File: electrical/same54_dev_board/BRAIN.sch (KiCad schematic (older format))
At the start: 8 parts, among them J2 Conn_ARM_JTAG_SWD_10, U1 p_ATSAME54P20A-AU, Y1 XOSC32

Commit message: Trying to figure out how I want to do power...
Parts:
- J2: footprint Connector_PinSocket_1.27mm:PinSocket_2x04_P1.27mm_Vertical -> Connector_PinHeader_1.27mm:PinHeader_2x05_P1.27mm_Vertical
- gave numbers to parts that had none: 5
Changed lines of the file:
@@
 F 0 "J2" H 5757 5196 50  0000 R CNN
 F 1 "Conn_ARM_JTAG_SWD_10" H 5757 5105 50  0000 R CNN
-F 2 "Connector_PinSocket_1.27mm:PinSocket_2x04_P1.27mm_Vertical" H 6200 5150 50  0001 C CNN
+F 2 "Connector_PinHeader_1.27mm:PinHeader_2x05_P1.27mm_Vertical" H 6200 5150 50  0001 C CNN
 F 3 "http://infocenter.arm.com/help/topic/com.arm.doc.ddi0314h/DDI0314H_coresight_components_trm.pdf" V 5850 3900 50  0001 C CNN
 	1    6200 5150
@@
 $EndComp
 $Comp
-L Device:C_Small C?
+L Device:C_Small C1
 U 1 1 5E7E5146
 P 5100 1050
-F 0 "C?" V 4871 1050 50  0000 C CNN
+F 0 "C1" V 4871 1050 50  0000 C CNN
 F 1 "6.8pF" V 4962 1050 50  0000 C CNN
 F 2 "" H 5100 1050 50  0001 C CNN
@@
 $EndComp
 $Comp
-L Device:C_Small C?
+L Device:C_Small C2
 U 1 1 5E7E6123
 P 5100 1550
-F 0 "C?" V 4871 1550 50  0000 C CNN
+F 0 "C2" V 4871 1550 50  0000 C CNN
 F 1 "6.8pF" V 4950 1500 50  0000 C CNN
 F 2 "" H 5100 1550 50  0001 C CNN
@@
 	5450 1300 5450 1550
 $Comp
-L power:GND #PWR?
+L power:GND #PWR0104
 U 1 1 5E825E8D
 P 5550 1300
-F 0 "#PWR?" H 5550 1050 50  0001 C CNN
+F 0 "#PWR0104" H 5550 1050 50  0001 C CNN
 F 1 "GND" H 5555 1127 50  0000 C CNN
 F 2 "" H 5550 1300 50  0001 C CNN
@@
 Connection ~ 5350 2700
 $Comp
-L power:GND #PWR?
+L power:GND #PWR0108
 U 1 1 5E880A2C
 P 5900 2850
-F 0 "#PWR?" H 5900 2600 50  0001 C CNN
+F 0 "#PWR0108" H 5900 2600 50  0001 C CNN
 F 1 "GND" H 5905 2677 50  0000 C CNN
 F 2 "" H 5900 2850 50  0001 C CNN
@@
 	4900 2750 4250 2750
 $Comp
-L Device:C_Small C?
+L Device:C_Small C5
 U 1 1 5E8AA0A3
 P 5250 3050
-F 0 "C?" V 5450 3050 50  0000 C CNN
+F 0 "C5" V 5450 3050 50  0000 C CNN
 F 1 "5pF" V 5350 3050 50  0000 C CNN
 F 2 "" H 5250 3050 50  0001 C CNN
@@
 	5350 2700 4950 2700
 $Comp
-L Device:Crystal_GND24 Y?
+L Device:Crystal_GND24 Y2
 U 1 1 5E843969
 P 5150 2700
-F 0 "Y?" V 5100 3050 50  0000 R CNN
+F 0 "Y2" V 5100 3050 50  0000 R CNN
 F 1 "XOSC0" V 5000 3200 50  0000 R CNN
 F 2 "" H 5150 2700 50  0001 C CNN
@@
 Connection ~ 5150 2900
 $Comp
-L Device:C_Small C?
+L Device:C_Small C4
 U 1 1 5E8C2D5D
 P 5250 2350
-F 0 "C?" V 5021 2350 50  0000 C CNN
+F 0 "C4" V 5021 2350 50  0000 C CNN
 F 1 "5pF" V 5112 2350 50  0000 C CNN
 F 2 "" H 5250 2350 50  0001 C CNN

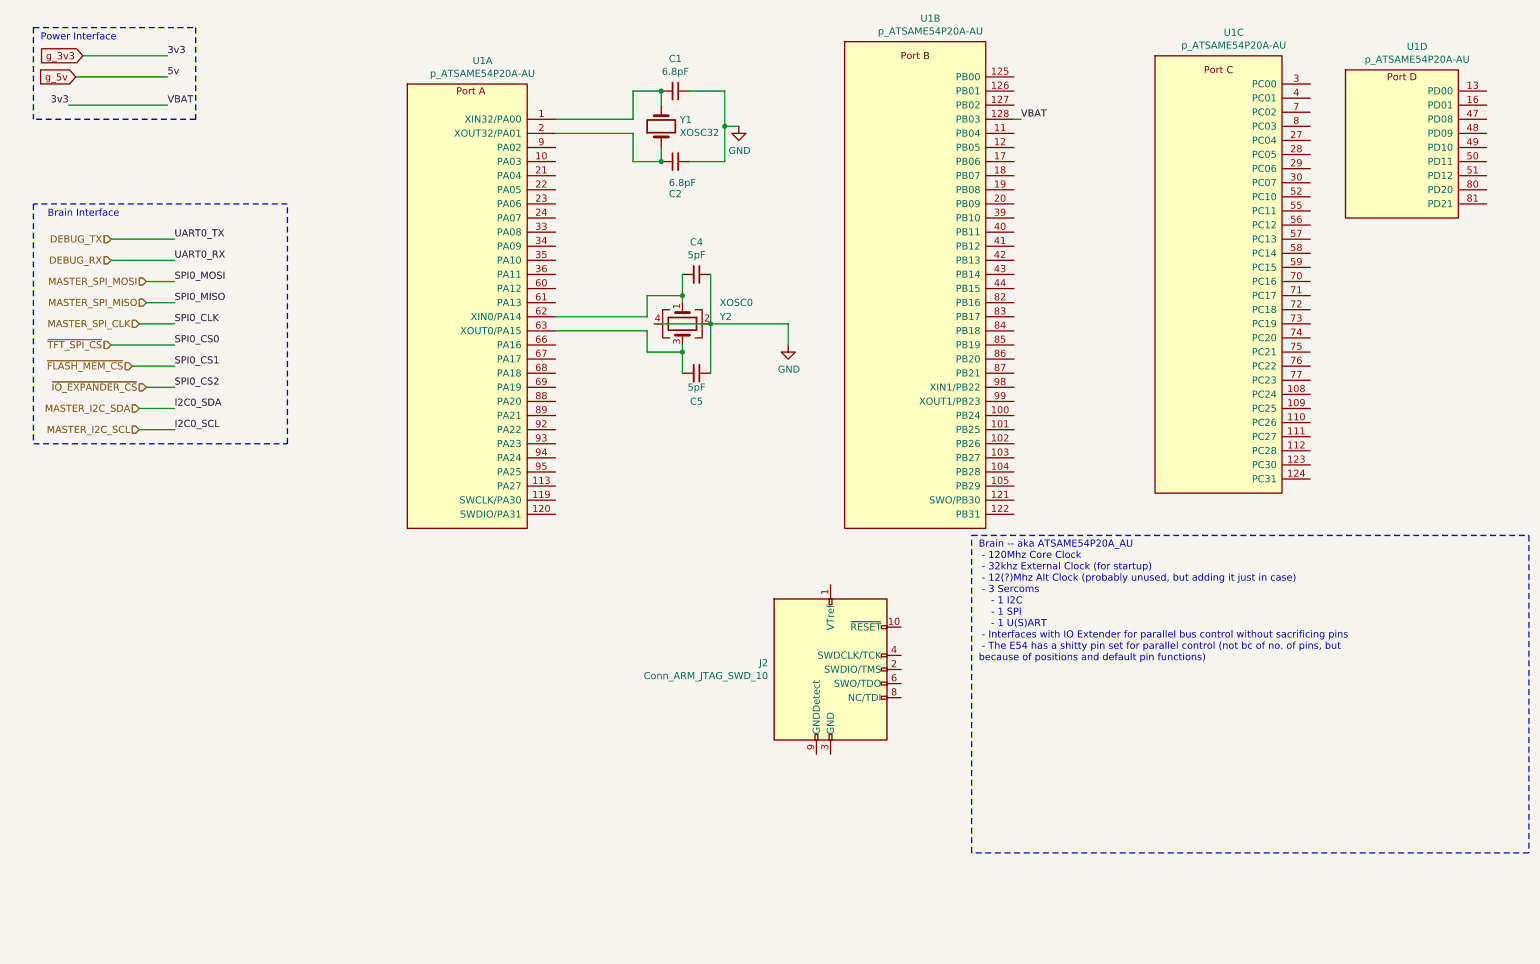
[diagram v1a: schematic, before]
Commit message: Added usart, i2c, and spi pin locations, as well as labeled sercoms
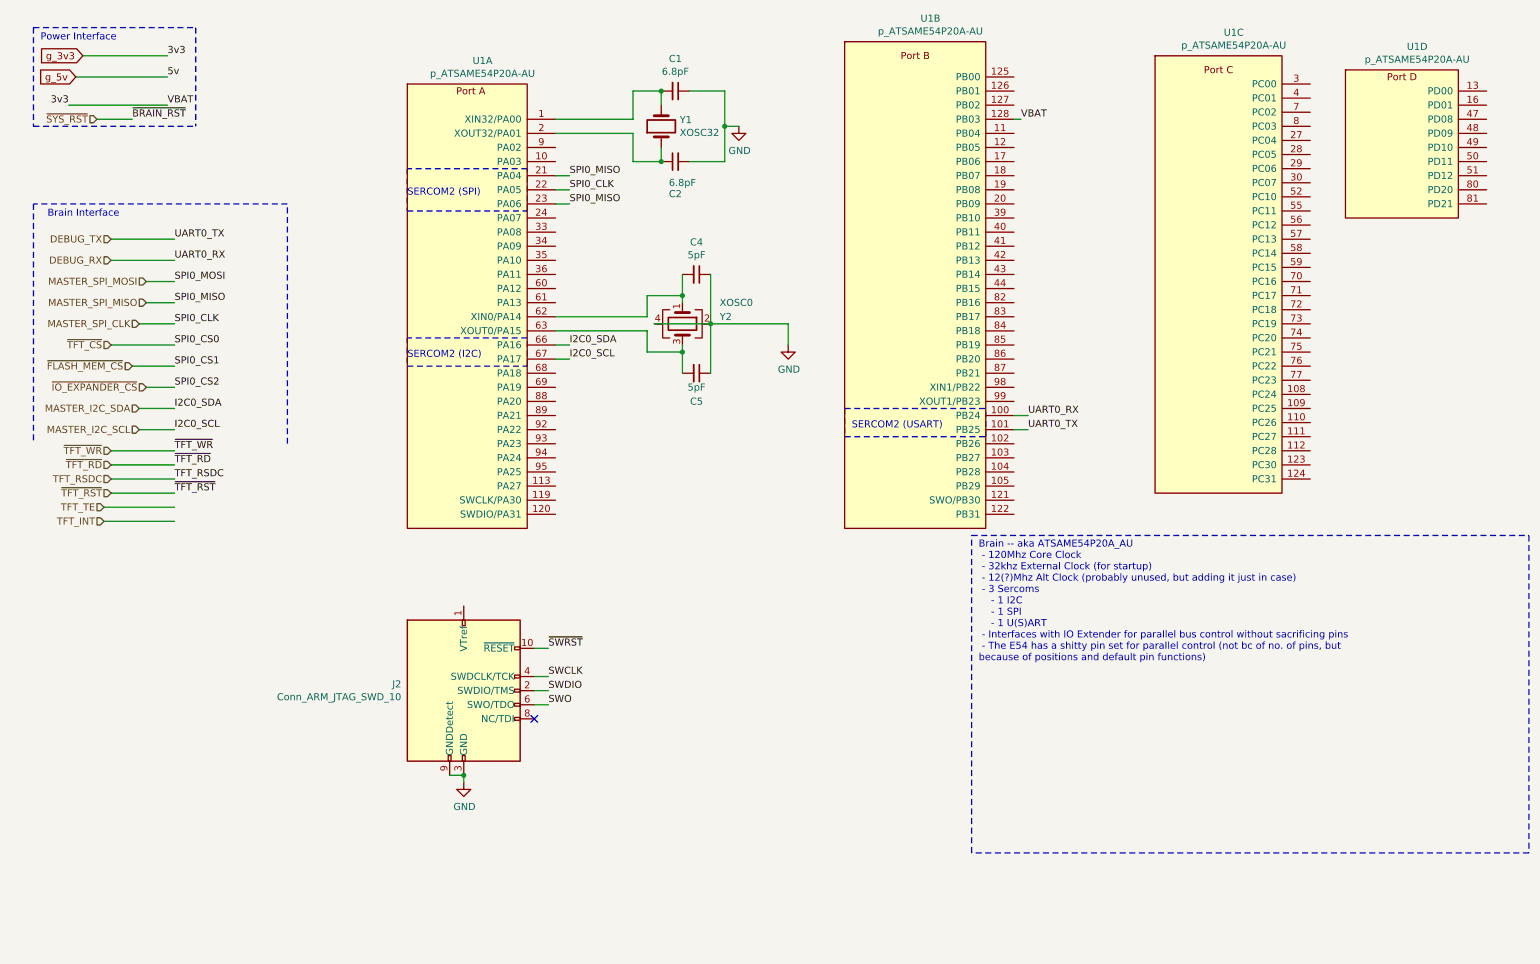
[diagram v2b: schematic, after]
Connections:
- net DEBUG_RX: now also U1.100 (PB24)
- net DEBUG_TX: now also U1.101 (PB25)
- net GND: now also J2.3 (GND), J2.5 (GND), J2.9 (GNDDetect)
- net MASTER_I2C_SCL: now also U1.67 (PA17)
- net MASTER_I2C_SDA: now also U1.66 (PA16)
- net MASTER_SPI_CLK: now also U1.22 (PA05)
- net MASTER_SPI_MISO: now also U1.21 (PA04), U1.23 (PA06)
- net ~SWRST: now reaches J2.10 (~RESET~)
- net SWDIO: now reaches J2.2 (SWDIO/TMS)
- net SWCLK: now reaches J2.4 (SWDCLK/TCK)
- net SWO: now reaches J2.6 (SWO/TDO)
- no-connect marks 0 -> 1
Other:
- note added: "SERCOM2 (I2C)"
- note added: "SERCOM2 (SPI)"
- note added: "SERCOM2 (USART)"
- moved on the sheet: J2
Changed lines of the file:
@@
 $Descr A4 11693 8268
 encoding utf-8
-Sheet 4 5
+Sheet 5 5
 Title ""
 Date ""
@@
 L Connector:Conn_ARM_JTAG_SWD_10 J2
 U 1 1 5EA1E350
-P 6200 5150
-F 0 "J2" H 5757 5196 50  0000 R CNN
-F 1 "Conn_ARM_JTAG_SWD_10" H 5757 5105 50  0000 R CNN
-F 2 "Connector_PinHeader_1.27mm:PinHeader_2x05_P1.27mm_Vertical" H 6200 5150 50  0001 C CNN
-F 3 "http://infocenter.arm.com/help/topic/com.arm.doc.ddi0314h/DDI0314H_coresight_components_trm.pdf" V 5850 3900 50  0001 C CNN
-	1    6200 5150
+P 3600 5300
+F 0 "J2" H 3157 5346 50  0000 R CNN
+F 1 "Conn_ARM_JTAG_SWD_10" H 3157 5255 50  0000 R CNN
+F 2 "Connector_PinHeader_1.27mm:PinHeader_2x05_P1.27mm_Vertical" H 3600 5300 50  0001 C CNN
+F 3 "http://infocenter.arm.com/help/topic/com.arm.doc.ddi0314h/DDI0314H_coresight_components_trm.pdf" V 3250 4050 50  0001 C CNN
+	1    3600 5300
 	1    0    0    -1
 $EndComp
@@
 MASTER_SPI_CLK
 Text HLabel 1100 2850 0    50   Input ~ 0
-~TFT_SPI_CS
+~TFT_CS
 Text HLabel 1250 3000 0    50   Input ~ 0
 ~FLASH_MEM_CS
@@
 Wire Notes Line
 	550  1850 550  3550
-Wire Notes Line
-	550  3550 2350 3550
 Wire Notes Line
 	2350 3550 2350 1850
@@
 Text Label 1500 1150 0    50   ~ 0
 VBAT
-Wire Notes Line
-	1700 1250 550  1250
-Wire Notes Line
-	1700 600  1700 1250
-Wire Notes Line
-	550  600  550  1250
 Wire Wire Line
 	7500 1250 7550 1250
+Text HLabel 1100 3600 0    50   Input ~ 0
+~TFT_WR
+Text HLabel 1100 3700 0    50   Input ~ 0
+~TFT_RD
+Text HLabel 1100 3800 0    50   Input ~ 0
+TFT_RSDC
+Wire Wire Line
+	1100 3600 1550 3600
+Wire Wire Line
+	1100 3700 1550 3700
+Wire Wire Line
+	1100 3800 1550 3800
+Text Label 1550 3600 0    50   ~ 0
+~TFT_WR
+Text Label 1550 3700 0    50   ~ 0
+~TFT_RD
+Text Label 1550 3800 0    50   ~ 0
+TFT_RSDC
+Text HLabel 1100 3900 0    50   Input ~ 0
+~TFT_RST
+Wire Wire Line
+	1100 3900 1550 3900
+Text Label 1550 3900 0    50   ~ 0
+~TFT_RST
+Text HLabel 1050 4000 0    50   Input ~ 0
+TFT_TE
+Text HLabel 1050 4100 0    50   Input ~ 0
+TFT_INT
+Wire Wire Line
+	1050 4100 1550 4100
+Wire Wire Line
+	1050 4000 1550 4000
+Wire Wire Line
+	4250 1850 4350 1850
+Wire Wire Line
+	4250 1750 4350 1750
+Wire Wire Line
+	4250 1650 4350 1650
+Text Label 4350 1750 0    50   ~ 0
+SPI0_CLK
+Text Label 4350 1850 0    50   ~ 0
+SPI0_MISO
+Text Label 4350 1650 0    50   ~ 0
+SPI0_MISO
+Wire Wire Line
+	7500 3350 7600 3350
+Wire Wire Line
+	7500 3450 7600 3450
+Text Label 7600 3450 0    50   ~ 0
+UART0_TX
+Text Label 7600 3350 0    50   ~ 0
+UART0_RX
+Text Notes 6350 3450 0    50   ~ 0
+SERCOM2 (USART)
+Wire Notes Line
+	6300 3500 7300 3500
+Wire Notes Line
+	7300 3500 7300 3300
+Wire Notes Line
+	6300 3300 7300 3300
+Wire Notes Line
+	6300 3300 6300 3500
+Wire Notes Line
+	4050 1600 3200 1600
+Wire Notes Line
+	3200 1600 3200 1900
+Wire Notes Line
+	3200 1900 4050 1900
+Wire Notes Line
+	4050 1900 4050 1600
+Text Notes 3200 1800 0    50   ~ 0
+SERCOM2 (SPI)
+Wire Wire Line
+	4250 2850 4350 2850
+Wire Wire Line
+	4250 2950 4350 2950
+Text Label 4350 2850 0    50   ~ 0
+I2C0_SDA
+Text Label 4350 2950 0    50   ~ 0
+I2C0_SCL
+Text Notes 3200 2950 0    50   ~ 0
+SERCOM2 (I2C)
+Wire Notes Line
+	4050 2800 3200 2800
+Wire Notes Line
+	3200 2800 3200 3000
+Wire Notes Line
+	3200 3000 4050 3000
+Wire Notes Line
+	4050 3000 4050 2800
+Wire Wire Line
+	4100 5000 4200 5000
+Text HLabel 1000 1250 0    50   Input ~ 0
+~SYS_RST
+Wire Notes Line
+	550  1300 1700 1300
+Wire Notes Line
+	1700 600  1700 1300
+Wire Notes Line
+	550  600  550  1300
+Text Label 1250 1250 0    50   ~ 0
+~BRAIN_RST
+Wire Wire Line
+	1000 1250 1250 1250
+Wire Wire Line
+	4100 5200 4200 5200
+Text Label 4200 5200 0    50   ~ 0
+SWCLK
+Wire Wire Line
+	4100 5300 4200 5300
+Text Label 4200 5300 0    50   ~ 0
+SWDIO
+Text Label 4200 5400 0    50   ~ 0
+SWO
+Wire Wire Line
+	4100 5400 4200 5400
+Wire Wire Line
+	3500 5900 3600 5900
+NoConn ~ 4100 5500
+Text Label 4200 5000 0    50   ~ 0
+~SWRST
+Wire Wire Line
+	3600 5900 3600 5950
+Connection ~ 3600 5900
+$Comp
+L power:GND #PWR?
+U 1 1 5EA9AF4B
+P 3600 5950
+F 0 "#PWR?" H 3600 5700 50  0001 C CNN
+F 1 "GND" H 3605 5777 50  0000 C CNN
+F 2 "" H 3600 5950 50  0001 C CNN
+F 3 "" H 3600 5950 50  0001 C CNN
+	1    3600 5950
+	1    0    0    -1
+$EndComp
 $EndSCHEMATC
